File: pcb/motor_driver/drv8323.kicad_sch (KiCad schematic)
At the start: 16 parts

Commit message: update pcb
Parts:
- removed C? (x2): 1u, Capacitor_SMD:C_0603_1608Metric_Pad1.08x0.95mm_HandSolder, symbol Device:C_Small
- removed C? (x2): 0.1u, Capacitor_SMD:C_0603_1608Metric_Pad1.08x0.95mm_HandSolder, symbol Device:C_Small
- removed C? (x3): 2200p, Capacitor_SMD:C_0603_1608Metric_Pad1.08x0.95mm_HandSolder, symbol Device:C_Small
- removed C?: 47n, Capacitor_SMD:C_0603_1608Metric_Pad1.08x0.95mm_HandSolder, symbol Device:C_Small
- removed D?: LED, LED_SMD:LED_0603_1608Metric_Pad1.05x0.95mm_HandSolder, symbol Device:LED
- removed R?: 1k, Resistor_SMD:R_0805_2012Metric_Pad1.20x1.40mm_HandSolder, symbol Device:R_Small
- removed R? (x3): 56, Resistor_SMD:R_0805_2012Metric_Pad1.20x1.40mm_HandSolder, symbol Device:R_Small
- removed R? (x2): 10k, Resistor_SMD:R_0603_1608Metric_Pad0.98x0.95mm_HandSolder, symbol Device:R_Small
- removed U?: DRV8323S, Package_DFN_QFN:QFN-40-1EP_6x6mm_P0.5mm_EP4.6x4.6mm_ThermalVias, symbol bldc_lib:DRV8323S
- added C1: 4.7u, Capacitor_SMD:C_0603_1608Metric_Pad1.08x0.95mm_HandSolder, symbol Device:C_Small
- added C10: 0.1u, Capacitor_SMD:C_0402_1005Metric_Pad0.74x0.62mm_HandSolder, symbol Device:C_Small
- added C11, C12, C13: 1n, Capacitor_SMD:C_0402_1005Metric_Pad0.74x0.62mm_HandSolder, symbol Device:C_Small
- added C2, C4: 1u, Capacitor_SMD:C_0603_1608Metric_Pad1.08x0.95mm_HandSolder, symbol Device:C_Small
- added C3: 0.047u, Capacitor_SMD:C_0603_1608Metric_Pad1.08x0.95mm_HandSolder, symbol Device:C_Small
- added C5, C6, C7: 0.1u, Capacitor_SMD:C_0603_1608Metric_Pad1.08x0.95mm_HandSolder, symbol Device:C_Small
- added C8: 150u, Capacitor_SMD:CP_Elec_8x10.5, symbol Device:C_Polarized_Small_US
- added C9: 10u, Capacitor_SMD:C_0603_1608Metric_Pad1.08x0.95mm_HandSolder, symbol Device:C_Small
- added D1, D2, D3: LED, LED_SMD:LED_0603_1608Metric_Pad1.05x0.95mm_HandSolder, symbol Device:LED
- added J2: 1-84953-1, bldc_lib:1-84953-1, symbol bldc_lib:1-84953-1
- added R1, R2, R3: 1k, Resistor_SMD:R_0402_1005Metric_Pad0.72x0.64mm_HandSolder, symbol Device:R_Small
- added R10, R11, R12, R4, R5, R6: 0, Resistor_SMD:R_0805_2012Metric_Pad1.20x1.40mm_HandSolder, symbol Device:R_Small
- added R7, R8, R9: 5m, Resistor_SMD:R_2010_5025Metric_Pad1.40x2.65mm_HandSolder, symbol Device:R_Small
- added U1, U2: USBLC6-4SC6, Package_TO_SOT_SMD:SOT-23-6, symbol Power_Protection:USBLC6-4SC6
- added U3: DRV8323S, Package_DFN_QFN:QFN-40-1EP_6x6mm_P0.5mm_EP4.6x4.6mm_ThermalVias, symbol bldc_lib:DRV8323S
- added U4: a1333, Package_SO:HTSSOP-14-1EP_4.4x5mm_P0.65mm_EP3.4x5mm_Mask3x3.1mm, symbol bldc_lib:a1333
- added U5, U6, U7: HP8K22TB, bldc_lib:HP8K24TB, symbol bldc_lib:HP8K22TB
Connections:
- net +3.3V: now also C6.1, U2.5 (VBUS), U3.33 (DVDD)
- net +BATT: now also C1.1, C2.1, C4.1, C8.1, C9.1, U3.4 (VM), U3.5 (VDRAIN), U5.10 (TR1_DRAIN4), U5.11 (TR1_DRAIN5), U5.2 (TR1_DRAIN1), U5.3 (TR1_DRAIN2), U5.4 (TR1_DRAIN3), U6.10 (TR1_DRAIN4), U6.11 (TR1_DRAIN5), U6.2 (TR1_DRAIN1), U6.3 (TR1_DRAIN2), U6.4 (TR1_DRAIN3), U7.10 (TR1_DRAIN4), U7.11 (TR1_DRAIN5), U7.2 (TR1_DRAIN1), U7.3 (TR1_DRAIN2), U7.4 (TR1_DRAIN3)
- net CAL: now also U3.31 (CAL)
- net ENABLE: now also U3.30 (ENABLE)
- net GHA: now also R4.1, U3.6 (GHA)
- net GHB: now also R5.1, U3.15 (GHB)
- net GHC: now also R6.1, U3.16 (GHC)
- net GLA: now also R10.2, U3.8 (GLA)
- net GLB: now also R11.2, U3.13 (GLB)
- net GLC: now also R12.2, U3.18 (GLC)
- net GND: now also C1.2, C10.2, C11.2, C12.2, C13.2, C2.2, C5.2, C6.2, C7.2, C8.2, C9.2, J2.5, J2.MP1, J2.MP2, R1.2, R2.2, R3.2, R7.1, R8.1, R9.1, U1.2 (GND), U1.4 (I/O3), U2.2 (GND), U3.10 (SNA), U3.11 (SNB), U3.20 (SNC), U3.32 (AGND), U3.40 (PGND), U4.5 (GND), U4.6 (GND), U4.7 (GND)
- net INHA: now also D1.2 (A), U3.34 (INHA)
- net INHB: now also D2.2 (A), U3.36 (INHB)
- net INHC: now also D3.2 (A), U3.38 (INHC)
- net INLA: now also U3.35 (INLA)
- net INLB: now also U3.37 (INLB)
- net INLC: now also U3.39 (INLC)
- net SHA: now also J2.6, J2.7, U3.7 (SHA), U5.9 (TR1_SOURCE/TR2_DRAIN)
- net SHB: now also J2.8, J2.9, U3.14 (SHB), U6.9 (TR1_SOURCE/TR2_DRAIN)
- net SHC: now also J2.10, J2.11, U3.17 (SHC), U7.9 (TR1_SOURCE/TR2_DRAIN)
- net SOA: now also U3.23 (SOA)
- net SOB: now also U3.22 (SOB)
- net SOC: now also U3.21 (SOC)
- new net: R11.1, U6.8 (TR2_GATE)
- new net: C7.1, U4.1 (BYP)
- new net: D1.1 (K), R1.1
- new net: R5.2, U6.1 (TR1_GATE)
- new net: R12.1, U7.8 (TR2_GATE)
- new net: R4.2, U5.1 (TR1_GATE)
- new net: D2.1 (K), R2.1
- new net: C4.2, U3.3 (VCP)
- new net: R6.2, U7.1 (TR1_GATE)
- new net: C3.1, U3.1 (CPL)
- new net: C3.2, U3.2 (CPH)
- new net: D3.1 (K), R3.1
- new net: R10.1, U5.8 (TR2_GATE)
- new net +3.3VA: C10.1, U3.24 (VREF)
- new net +5V: C5.1, J2.1, U1.5 (VBUS), U4.2 (VCC)
- new net FAULTB: U3.25 (nFAULT)
- new net HALL_U: J2.3, U1.1 (I/O1)
- new net HALL_V: J2.4, U1.3 (I/O2)
- new net HALL_W: J2.2, U1.6 (I/O4)
- new net SLA: C11.1, R7.2, U3.9 (SPA), U5.5 (TR2_SOURCE1), U5.6 (TR2_SOURCE2), U5.7 (TR2_SOURCE3)
- new net SLB: C12.1, R8.2, U3.12 (SPB), U6.5 (TR2_SOURCE1), U6.6 (TR2_SOURCE2), U6.7 (TR2_SOURCE3)
- new net SLC: C13.1, R9.2, U3.19 (SPC), U7.5 (TR2_SOURCE1), U7.6 (TR2_SOURCE2), U7.7 (TR2_SOURCE3)
- new net SPI1_CLK: U2.1 (I/O1), U3.28 (SCLK), U4.9 (SCLK)
- new net SPI1_MISO: U2.6 (I/O4), U3.26 (SDO), U4.11 (MISO)
- new net SPI1_MOSI: U2.3 (I/O2), U3.27 (SDI), U4.10 (MOSI_SA1)
- new net SS_DRV: U3.29 (nSCS)
- new net SS_ENC: U2.4 (I/O3), U4.8 (CS/SA0)
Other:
- removed sheet half_bridge1
- note added: "Cap"
- note added: "DRV"
- note added: "Driver Stage"
- note added: "Encoder"
- note added: "Motor Connector"

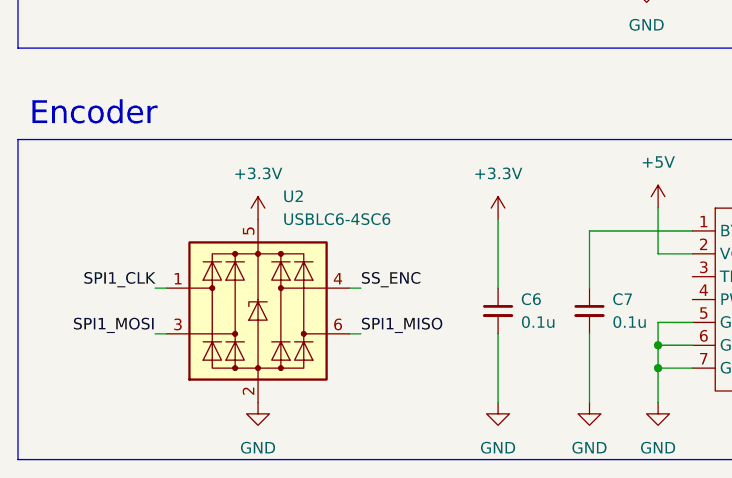
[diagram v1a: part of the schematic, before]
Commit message: delete ESD protection
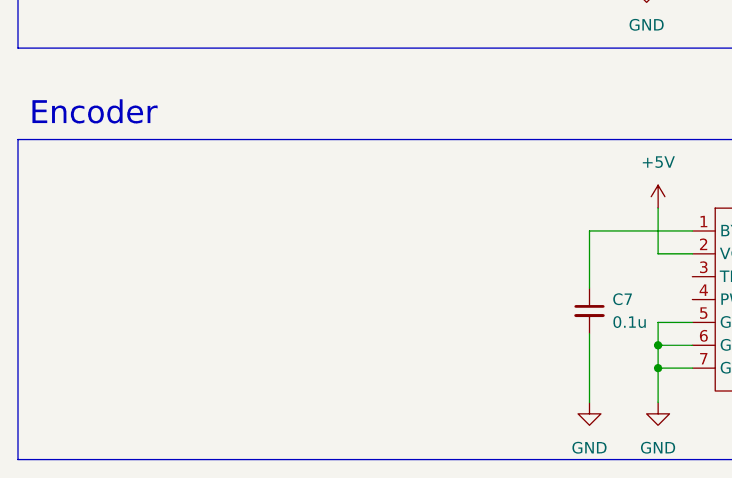
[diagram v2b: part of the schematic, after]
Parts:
- removed C6: 0.1u, Capacitor_SMD:C_0603_1608Metric_Pad1.08x0.95mm_HandSolder, symbol Device:C_Small
- removed U2: USBLC6-4SC6, Package_TO_SOT_SMD:SOT-23-6, symbol Power_Protection:USBLC6-4SC6
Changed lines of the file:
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@@
-    (stroke (width 0) (type default) (color 0 0 0 0))
-  )
-  (wire (pts (xy 33.02 173.99) (xy 34.29 173.99))
     (stroke (width 0) (type default) (color 0 0 0 0))
   )
@@
     (stroke (width 0) (type default) (color 0 0 0 0))
   )
-  (wire (pts (xy 54.61 173.99) (xy 55.88 173.99))
-    (stroke (width 0) (type default) (color 0 0 0 0))
-  )
   (wire (pts (xy 200.66 113.03) (xy 207.01 113.03))
     (stroke (width 0) (type default) (color 0 0 0 0))
@@
     (stroke (width 0) (type default) (color 0 0 0 0))
   )
-  (wire (pts (xy 71.12 166.37) (xy 71.12 173.99))
-    (stroke (width 0) (type default) (color 0 0 0 0))
-  )
   (wire (pts (xy 267.97 85.09) (xy 267.97 86.36))
     (stroke (width 0) (type default) (color 0 0 0 0))
@@
     (stroke (width 0) (type default) (color 0 0 0 0))
   )
-  (wire (pts (xy 33.02 179.07) (xy 34.29 179.07))
-    (stroke (width 0) (type default) (color 0 0 0 0))
-  )
   (wire (pts (xy 250.19 41.91) (xy 254 41.91))
     (stroke (width 0) (type default) (color 0 0 0 0))
@@
     (stroke (width 0) (type default) (color 0 0 0 0))
   )
-  (wire (pts (xy 54.61 179.07) (xy 55.88 179.07))
-    (stroke (width 0) (type default) (color 0 0 0 0))
-  )
   (wire (pts (xy 151.13 46.99) (xy 151.13 50.8))
     (stroke (width 0) (type default) (color 0 0 0 0))
@@
   )
   (wire (pts (xy 265.43 66.04) (xy 260.35 66.04))
-    (stroke (width 0) (type default) (color 0 0 0 0))
-  )
-  (wire (pts (xy 71.12 179.07) (xy 71.12 186.69))
     (stroke (width 0) (type default) (color 0 0 0 0))
   )
@@
     (effects (font (size 1.27 1.27)) (justify left bottom))
   )
-  (label "SPI1_MISO" (at 55.88 179.07 0)
-    (effects (font (size 1.27 1.27)) (justify left bottom))
-  )
   (label "SPI1_MOSI" (at 121.92 55.88 180)
     (effects (font (size 1.27 1.27)) (justify right bottom))
@@
     (effects (font (size 1.27 1.27)) (justify left bottom))
   )
-  (label "SPI1_MOSI" (at 33.02 179.07 180)
-    (effects (font (size 1.27 1.27)) (justify right bottom))
-  )
-  (label "SS_ENC" (at 55.88 173.99 0)
-    (effects (font (size 1.27 1.27)) (justify left bottom))
-  )
   (label "GLB" (at 265.43 66.04 180)
     (effects (font (size 1.27 1.27)) (justify right bottom))
@@
   (label "GHC" (at 88.9 88.9 90)
     (effects (font (size 1.27 1.27)) (justify left bottom))
-  )
-  (label "SPI1_CLK" (at 33.02 173.99 180)
-    (effects (font (size 1.27 1.27)) (justify right bottom))
   )
   (label "GHB" (at 189.23 66.04 0)
@@
     (pin "1")
     (pin "2")
-  )
-  (symbol (lib_id "power:GND") (at 44.45 186.69 0) (unit 1)
-    (in_bom yes) (on_board yes) (fields_autoplaced)
-    (property "Reference" "#PWR08" (id 0) (at 44.45 193.04 0)
-      (effects (font (size 1.27 1.27)) hide)
-    )
-    (property "Value" "GND" (id 1) (at 44.45 191.77 0))
-    (property "Footprint" "" (id 2) (at 44.45 186.69 0)
-      (effects (font (size 1.27 1.27)) hide)
-    )
-    (property "Datasheet" "" (id 3) (at 44.45 186.69 0)
-      (effects (font (size 1.27 1.27)) hide)
-    )
-    (pin "1")
   )
   (symbol (lib_id "Device:LED") (at 140.97 43.18 90) (unit 1)
@@
     (pin "2")
   )
-  (symbol (lib_id "Device:C_Small") (at 71.12 176.53 0) (unit 1)
-    (in_bom yes) (on_board yes) (fields_autoplaced)
-    (property "Reference" "C6" (id 0) (at 73.66 175.2662 0)
-      (effects (font (size 1.27 1.27)) (justify left))
-    )
-    (property "Value" "0.1u" (id 1) (at 73.66 177.8062 0)
-      (effects (font (size 1.27 1.27)) (justify left))
-    )
-    (property "Footprint" "Capacitor_SMD:C_0603_1608Metric_Pad1.08x0.95mm_HandSolder" (id 2) (at 71.12 176.53 0)
-      (effects (font (size 1.27 1.27)) hide)
-    )
-    (property "Datasheet" "~" (id 3) (at 71.12 176.53 0)
-      (effects (font (size 1.27 1.27)) hide)
-    )
-    (pin "1")
-    (pin "2")
-  )
-  (symbol (lib_id "power:GND") (at 71.12 186.69 0) (unit 1)
-    (in_bom yes) (on_board yes) (fields_autoplaced)
-    (property "Reference" "#PWR014" (id 0) (at 71.12 193.04 0)
-      (effects (font (size 1.27 1.27)) hide)
-    )
-    (property "Value" "GND" (id 1) (at 71.12 191.77 0))
-    (property "Footprint" "" (id 2) (at 71.12 186.69 0)
-      (effects (font (size 1.27 1.27)) hide)
-    )
-    (property "Datasheet" "" (id 3) (at 71.12 186.69 0)
-      (effects (font (size 1.27 1.27)) hide)
-    )
-    (pin "1")
-  )
   (symbol (lib_id "Device:R_Small") (at 151.13 53.34 0) (unit 1)
     (in_bom yes) (on_board yes) (fields_autoplaced)
@@
     (pin "2")
   )
-  (symbol (lib_name "+3.3V_1") (lib_id "power:+3.3V") (at 44.45 166.37 0) (unit 1)
-    (in_bom yes) (on_board yes) (fields_autoplaced)
-    (property "Reference" "#PWR0101" (id 0) (at 44.45 170.18 0)
-      (effects (font (size 1.27 1.27)) hide)
-    )
-    (property "Value" "+3.3V" (id 1) (at 44.45 161.29 0))
-    (property "Footprint" "" (id 2) (at 44.45 166.37 0)
-      (effects (font (size 1.27 1.27)) hide)
-    )
-    (property "Datasheet" "" (id 3) (at 44.45 166.37 0)
-      (effects (font (size 1.27 1.27)) hide)
-    )
-    (pin "1")
-  )
   (symbol (lib_id "power:+5V") (at 124.46 110.49 0) (unit 1)
     (in_bom yes) (on_board yes) (fields_autoplaced)
@@
       (effects (font (size 1.27 1.27)) hide)
     )
-    (pin "1")
-    (pin "2")
-    (pin "3")
-    (pin "4")
-    (pin "5")
-    (pin "6")
-  )
-  (symbol (lib_name "+3.3V_1") (lib_id "power:+3.3V") (at 71.12 166.37 0) (unit 1)
-    (in_bom yes) (on_board yes) (fields_autoplaced)
-    (property "Reference" "#PWR0102" (id 0) (at 71.12 170.18 0)
-      (effects (font (size 1.27 1.27)) hide)
-    )
-    (property "Value" "+3.3V" (id 1) (at 71.12 161.29 0))
-    (property "Footprint" "" (id 2) (at 71.12 166.37 0)
-      (effects (font (size 1.27 1.27)) hide)
-    )
-    (property "Datasheet" "" (id 3) (at 71.12 166.37 0)
-      (effects (font (size 1.27 1.27)) hide)
-    )
-    (pin "1")
-  )
-  (symbol (lib_id "Power_Protection:USBLC6-4SC6") (at 44.45 176.53 0) (unit 1)
-    (in_bom yes) (on_board yes) (fields_autoplaced)
-    (property "Reference" "U2" (id 0) (at 47.2187 163.83 0)
-      (effects (font (size 1.27 1.27)) (justify left))
-    )
-    (property "Value" "USBLC6-4SC6" (id 1) (at 47.2187 166.37 0)
-      (effects (font (size 1.27 1.27)) (justify left))
-    )
-    (property "Footprint" "Package_TO_SOT_SMD:SOT-23-6" (id 2) (at 44.45 189.23 0)
-      (effects (font (size 1.27 1.27)) hide)
-    )
-    (property "Datasheet" "https://www.st.com/resource/en/datasheet/usblc6-4.pdf" (id 3) (at 49.53 167.64 0)
-      (effects (font (size 1.27 1.27)) hide)
-    )

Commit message: update pcb
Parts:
- renumbered U5 to Q2, U6 to Q3, U7 to Q4
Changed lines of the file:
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@@
   (symbol (lib_id "bldc_lib:HP8K22TB") (at 227.33 59.69 0) (unit 1)
     (in_bom yes) (on_board yes) (fields_autoplaced)
-    (property "Reference" "U6" (id 0) (at 227.965 58.42 0))
+    (property "Reference" "Q3" (id 0) (at 227.965 58.42 0))
     (property "Value" "HP8K22TB" (id 1) (at 227.965 60.96 0))
     (property "Footprint" "bldc_lib:HP8K24TB" (id 2) (at 227.33 59.69 0)
@@
   (symbol (lib_id "bldc_lib:HP8K22TB") (at 228.6 93.98 0) (unit 1)
     (in_bom yes) (on_board yes) (fields_autoplaced)
-    (property "Reference" "U7" (id 0) (at 229.235 92.71 0))
+    (property "Reference" "Q4" (id 0) (at 229.235 92.71 0))
     (property "Value" "HP8K22TB" (id 1) (at 229.235 95.25 0))
     (property "Footprint" "bldc_lib:HP8K24TB" (id 2) (at 228.6 93.98 0)
@@
   (symbol (lib_id "bldc_lib:HP8K22TB") (at 227.33 25.4 0) (unit 1)
     (in_bom yes) (on_board yes) (fields_autoplaced)
-    (property "Reference" "U5" (id 0) (at 227.965 24.13 0))
+    (property "Reference" "Q2" (id 0) (at 227.965 24.13 0))
     (property "Value" "HP8K22TB" (id 1) (at 227.965 26.67 0))
     (property "Footprint" "bldc_lib:HP8K24TB" (id 2) (at 227.33 25.4 0)

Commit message: chore: add circuit git changes
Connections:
- net GND: now also U3.41 (GND), U4.15 (GND)

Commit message: feat: fix most bug
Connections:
- net +5V: now also J2.11; no longer J2.1
- net GND: now also J2.7; no longer J2.5
- net HALL_U: now also J2.9; no longer J2.3
- net HALL_V: now also J2.8; no longer J2.4
- net HALL_W: now also J2.10; no longer J2.2
- net SHA: now also J2.5; no longer J2.7
- net SHB: now also J2.3, J2.4; no longer J2.8, J2.9
- net SHC: now also J2.1, J2.2; no longer J2.10, J2.11
- net SPI1_CLK: no longer U4.9 (SCLK)
- net SPI1_MISO: no longer U4.11 (MISO)
- net SPI1_MOSI: no longer U4.10 (MOSI_SA1)
- new net SPI2_CLK: U4.9 (SCLK)
- new net SPI2_MISO: U4.11 (MISO)
- new net SPI2_MOSI: U4.10 (MOSI_SA1)

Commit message: chore: commit before starting to develop v1.2
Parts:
- removed C5: 0.1u, Capacitor_SMD:C_0603_1608Metric_Pad1.08x0.95mm_HandSolder, symbol Device:C_Small
- removed D1, D2, D3: LED, LED_SMD:LED_0603_1608Metric_Pad1.05x0.95mm_HandSolder, symbol Device:LED
- removed R1, R2, R3: 1k, Resistor_SMD:R_0402_1005Metric_Pad0.72x0.64mm_HandSolder, symbol Device:R_Small
- removed U1: USBLC6-4SC6, Package_TO_SOT_SMD:SOT-23-6, symbol Power_Protection:USBLC6-4SC6
- added C6: 1u, Capacitor_SMD:C_0603_1608Metric_Pad1.08x0.95mm_HandSolder, symbol Device:C_Small
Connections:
- net GND: now also C6.1
- net +3.3V: no longer names the net of U3.33 (DVDD)
- net +3.3V: now also C6.2
